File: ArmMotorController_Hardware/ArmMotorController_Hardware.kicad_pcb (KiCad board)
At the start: 2 copper layers, 124.5 x 121.9 mm, 110 parts, among them SW1 SW_Push, SW2 SW_Push, SW3 SW_Push, SW4 SW_Push, SW5 SW_SPDT, U1 AP1059, U2 AP1059, U3 TM4C129E_Launchpad, U4 MAX_3232, U5 VNH5019A_E, U6 VNH5019A_E, U7 VNH5019A_E, U8 VNH5019A_E

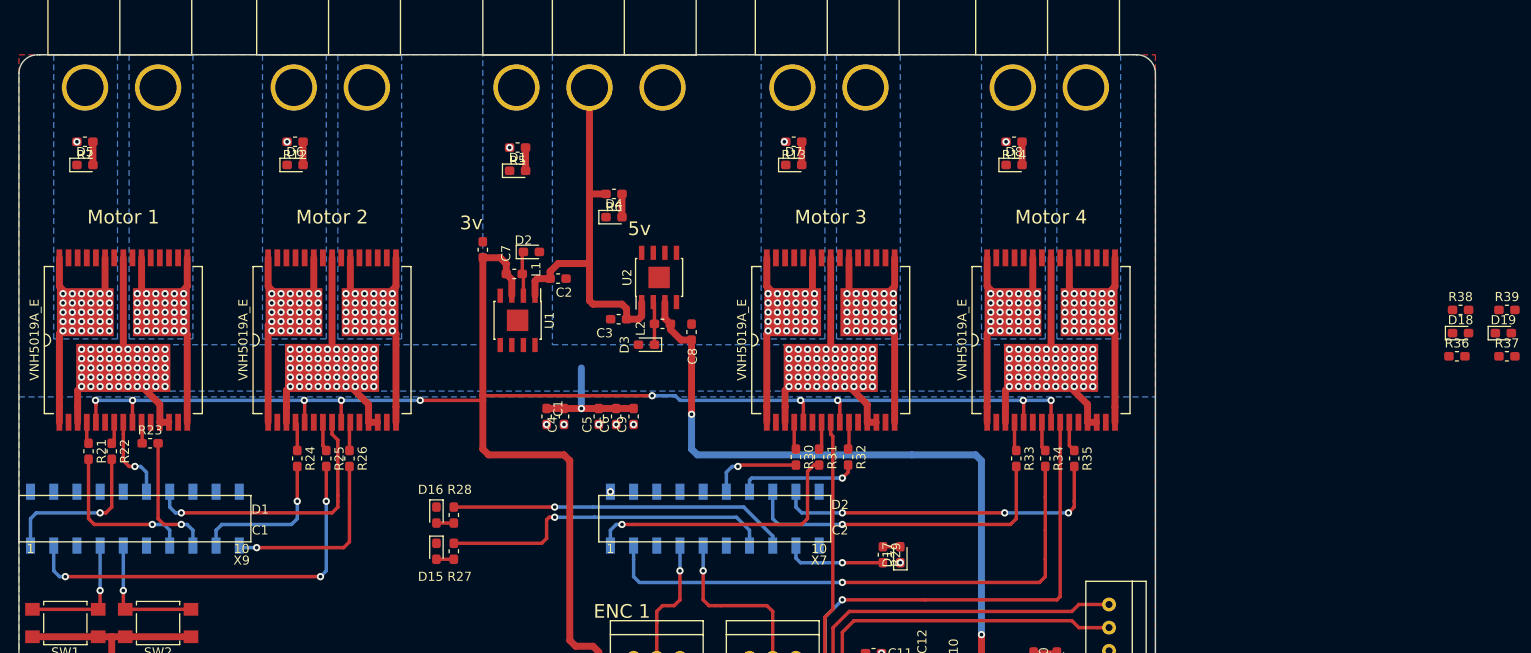
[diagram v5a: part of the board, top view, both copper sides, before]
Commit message: Began moving the new schematic change into place and added a junction to the schematic
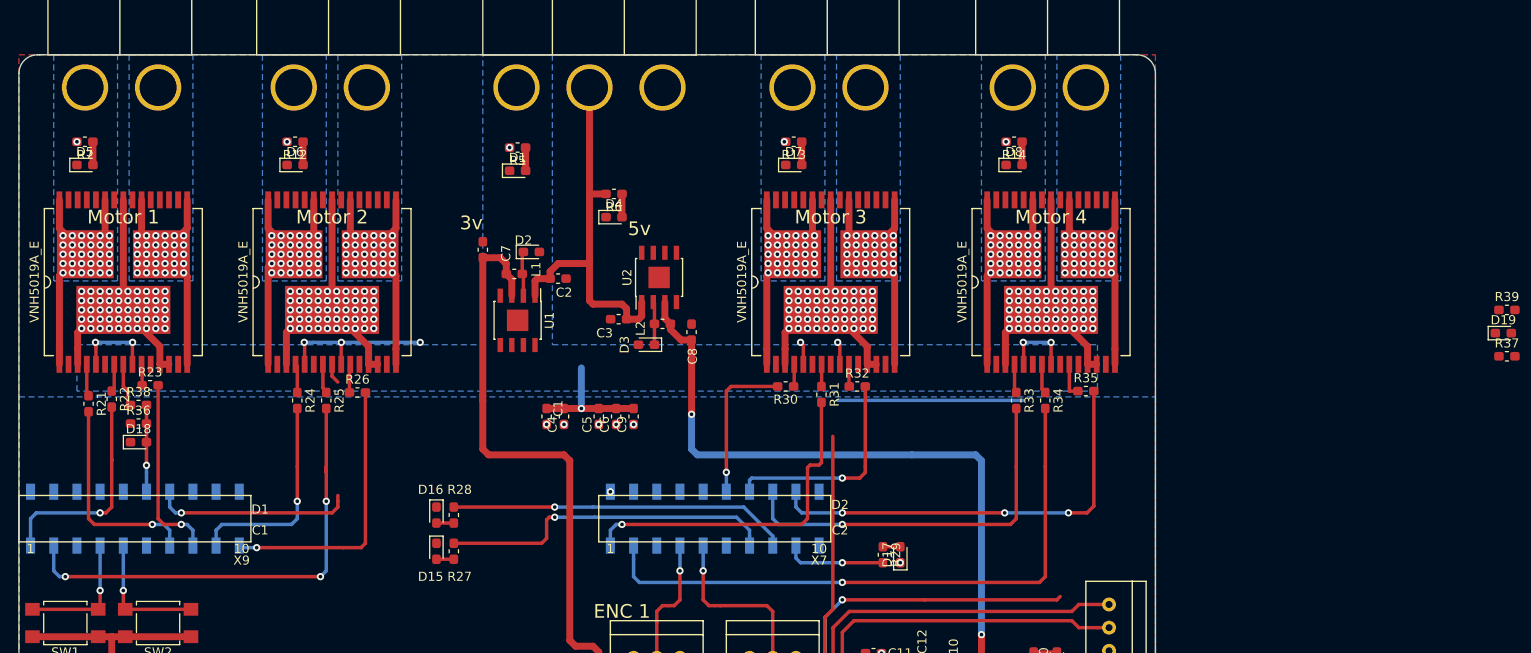
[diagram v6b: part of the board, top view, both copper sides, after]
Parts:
- moved D18 145.3 mm to (52.5, 84.3)
- moved R38 145.2 mm to (52.5, 80.3)
- moved R36 144.6 mm to (52.5, 82.3)
- moved R30 7.81 mm to (123.3, 78.2), turned to 180 degrees
- moved R32 7.80 mm to (131.2, 78.2), turned to 0 degrees
- moved R35 7.49 mm to (156.2, 78.7), turned to 0 degrees
- moved R26 7.28 mm to (76.4, 78.9), turned to 0 degrees
- moved R31 6.86 mm to (127.3, 79.1)
- moved R24 6.35 mm to (69.8, 79.8)
- moved R25 6.35 mm to (73.0, 79.8)
- moved R33 6.35 mm to (148.6, 79.8)
- moved R34 6.35 mm to (151.8, 79.8)
- moved R23 6.35 mm to (53.7, 78.1)
- moved U5 6.35 mm to (50.8, 66.8)
- moved U6 6.35 mm to (73.7, 66.8)
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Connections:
- D18 pad 2: Net-(D18-Pad2) -> I_Sense_1
- D19 pad 2: Net-(D19-Pad2) -> I_Sense_2
- D20 pad 2: Net-(D20-Pad2) -> I_Sense_3
- D21 pad 2: Net-(D21-Pad2) -> I_Sense_4
- R36 pad 2: Net-(D18-Pad2) -> I_Sense_1
- R37 pad 2: Net-(D19-Pad2) -> I_Sense_2
- R40 pad 2: Net-(D20-Pad2) -> I_Sense_3
- R41 pad 2: Net-(D21-Pad2) -> I_Sense_4
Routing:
- net +3V3: track 454.6 -> 389.9 mm, vias 12 -> 11
- net I_Sense_4: track 85.3 -> 66.2 mm
- net IN_B3: track 13.2 -> 23.7 mm
- net IN_B4: track 37.1 -> 47.5 mm
- net IN_B2: track 20.7 -> 30.6 mm
- net I_Sense_2: track 30.2 -> 21.9 mm
- net Mo3_PWM: track 30.5 -> 37.7 mm
- net Mo2_PWM: track 44.6 -> 51.6 mm
- net IN_A3: track 10.1 -> 16.9 mm
- net Mo4_PWM: track 61.1 -> 67.4 mm
- net IN_A4: track 35.9 -> 42.2 mm
- net IN_A2: track 16.8 -> 23.2 mm
- net IN_B1: track 14.3 -> 20.6 mm
- net Mo1_PWM: track 17.6 -> 23.5 mm
- net IN_A1: track 17.2 -> 22.8 mm
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
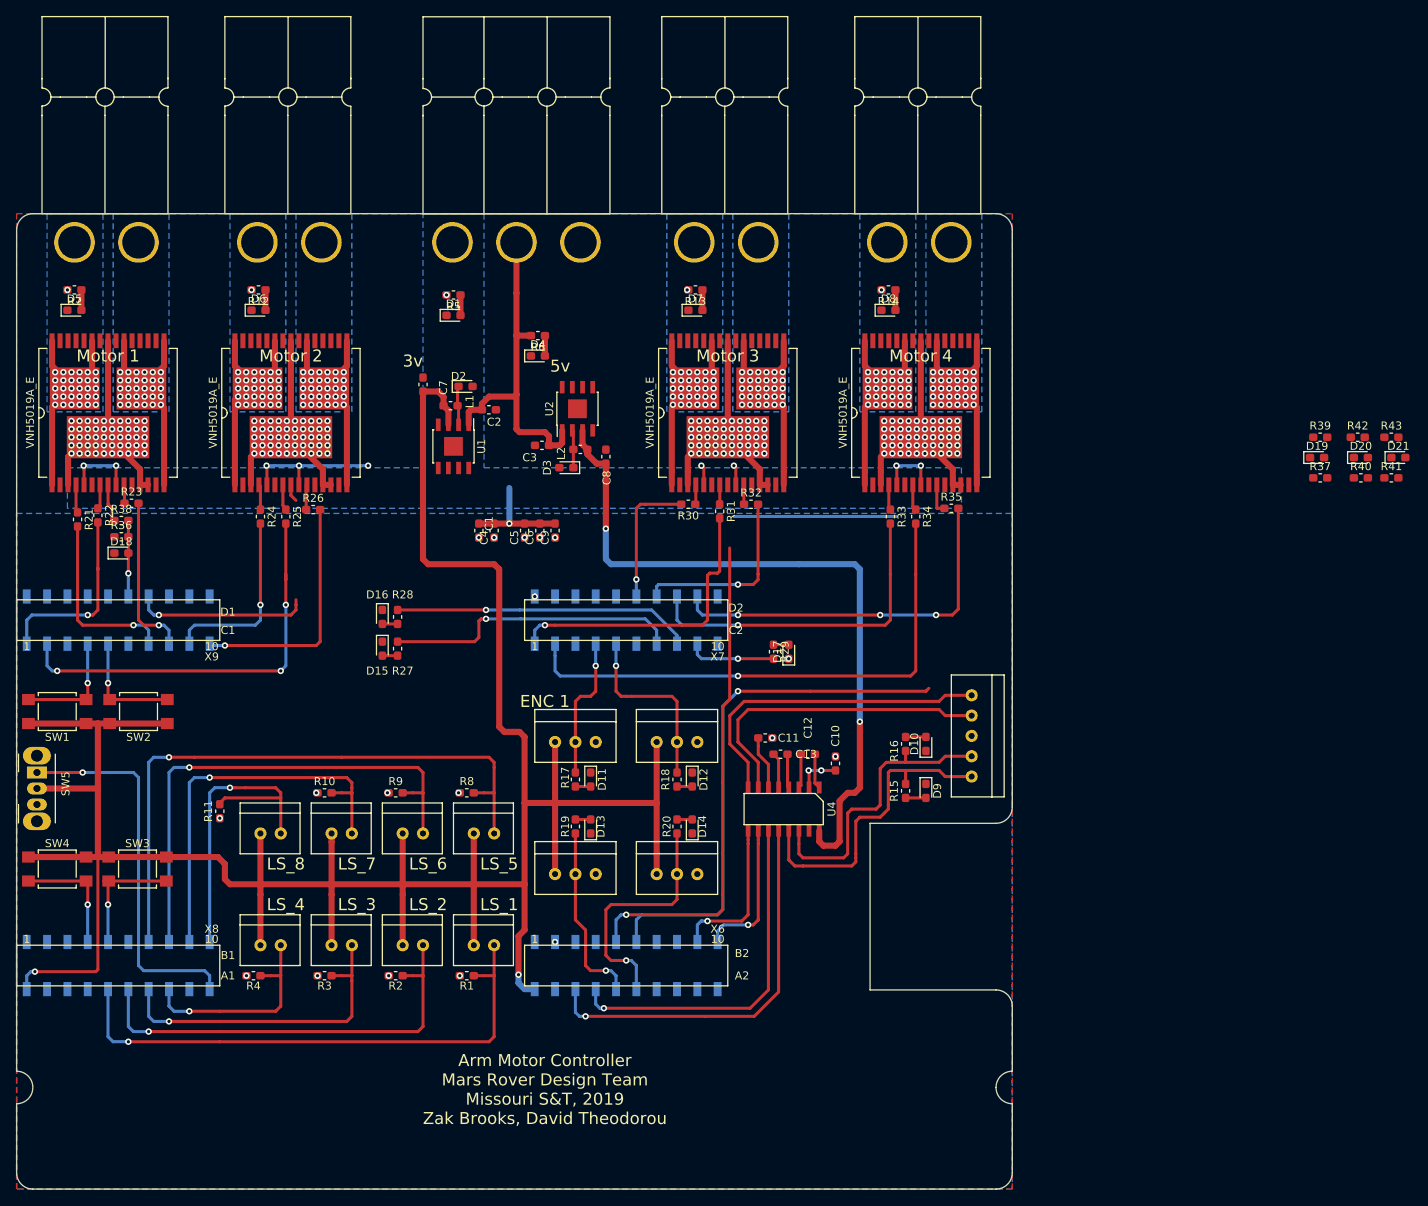
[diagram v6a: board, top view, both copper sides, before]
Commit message: Finished attaching the new circuit and made sure everything was connected
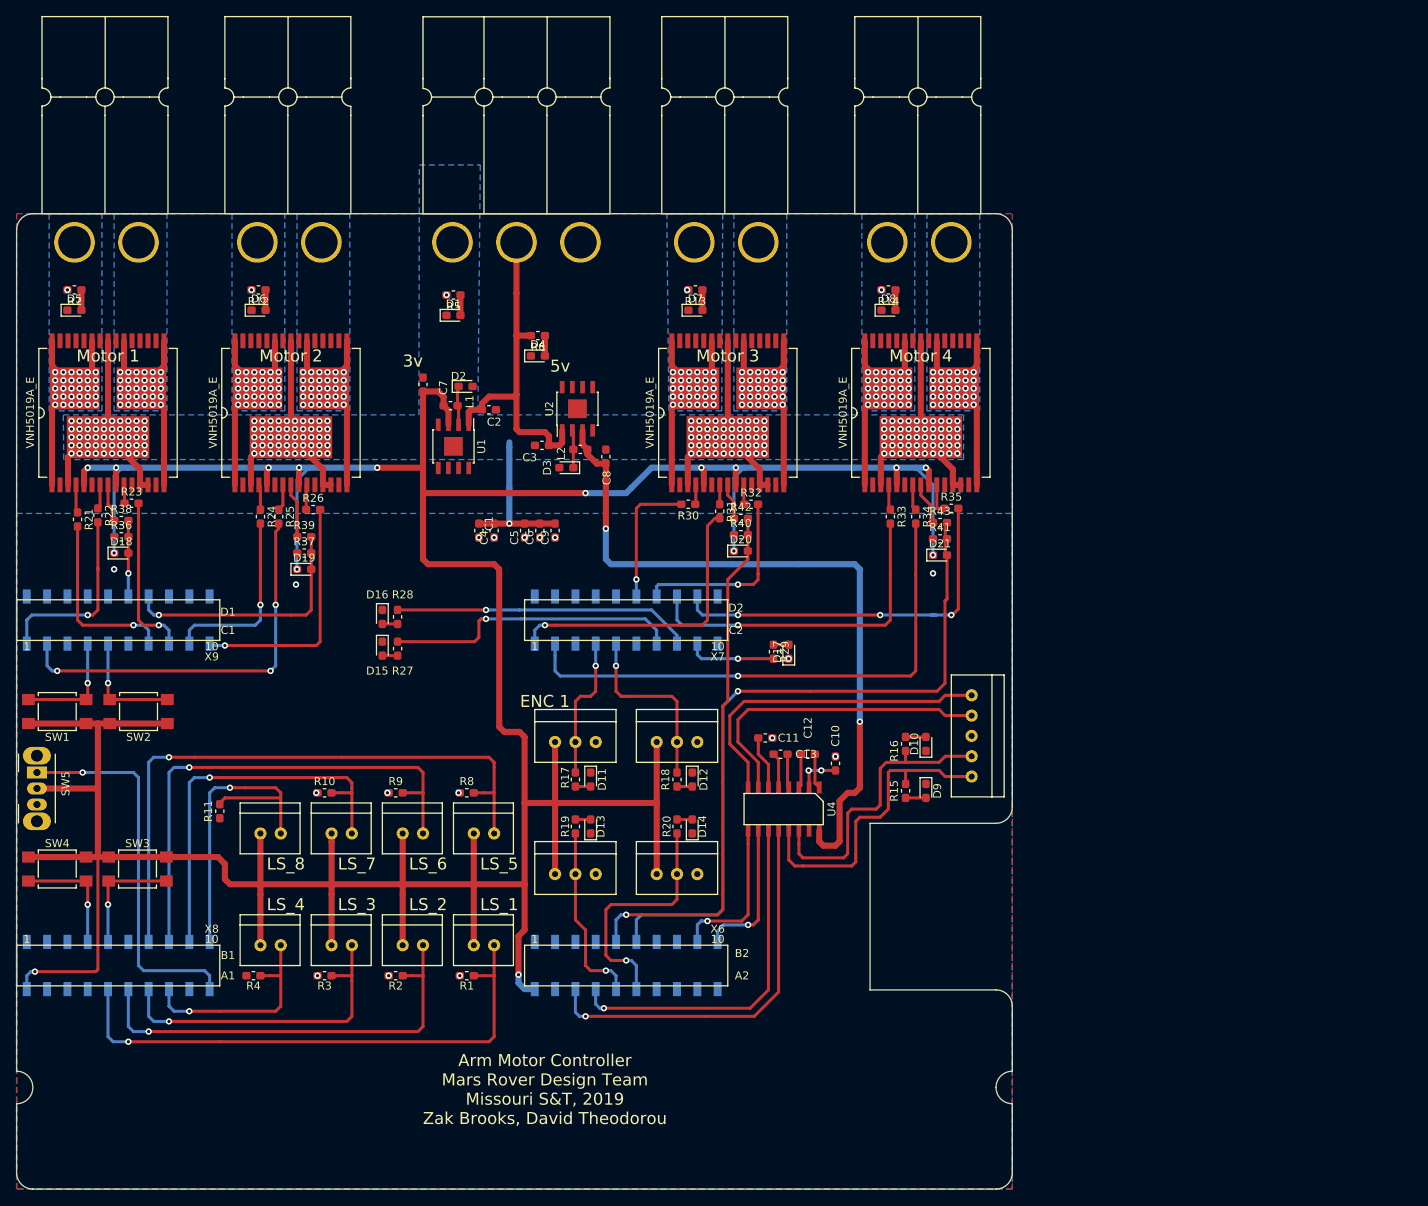
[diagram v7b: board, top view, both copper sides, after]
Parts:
- moved R39 127.6 mm to (75.3, 82.3)
- moved D19 127.4 mm to (75.3, 86.4)
- moved R37 127.3 mm to (75.3, 84.3)
- moved D20 78.4 mm to (129.9, 84.1)
- moved R40 77.8 mm to (129.9, 82.0)
- moved R42 77.8 mm to (129.9, 80.0)
- moved D21 58.6 mm to (154.8, 84.6)
- moved R43 57.4 mm to (154.8, 80.5)
- moved R41 56.9 mm to (154.8, 82.5)
- moved R25 0.89 mm to (72.1, 79.8)
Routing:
- net +3V3: track 389.9 -> 501.3 mm, vias 11 -> 16
- net I_Sense_4: track 66.2 -> 88.7 mm
- net I_Sense_2: track 21.9 -> 31.7 mm
- net 12vAct: track 136.2 -> 141.9 mm
- net Net-(R43-Pad1): track 0.00 -> 5.25 mm
- net I_Sense_3: track 62.2 -> 66.8 mm
- net Net-(R39-Pad1): track 2.21 -> 6.82 mm
- net Net-(R42-Pad1): track 0.00 -> 4.52 mm
- net Mo2_PWM: track 51.6 -> 49.8 mm
- net IN_B4: track 47.5 -> 48.1 mm
- net GND: vias 19 -> 18

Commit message: FInished the schematic changes and attched them on the PCB
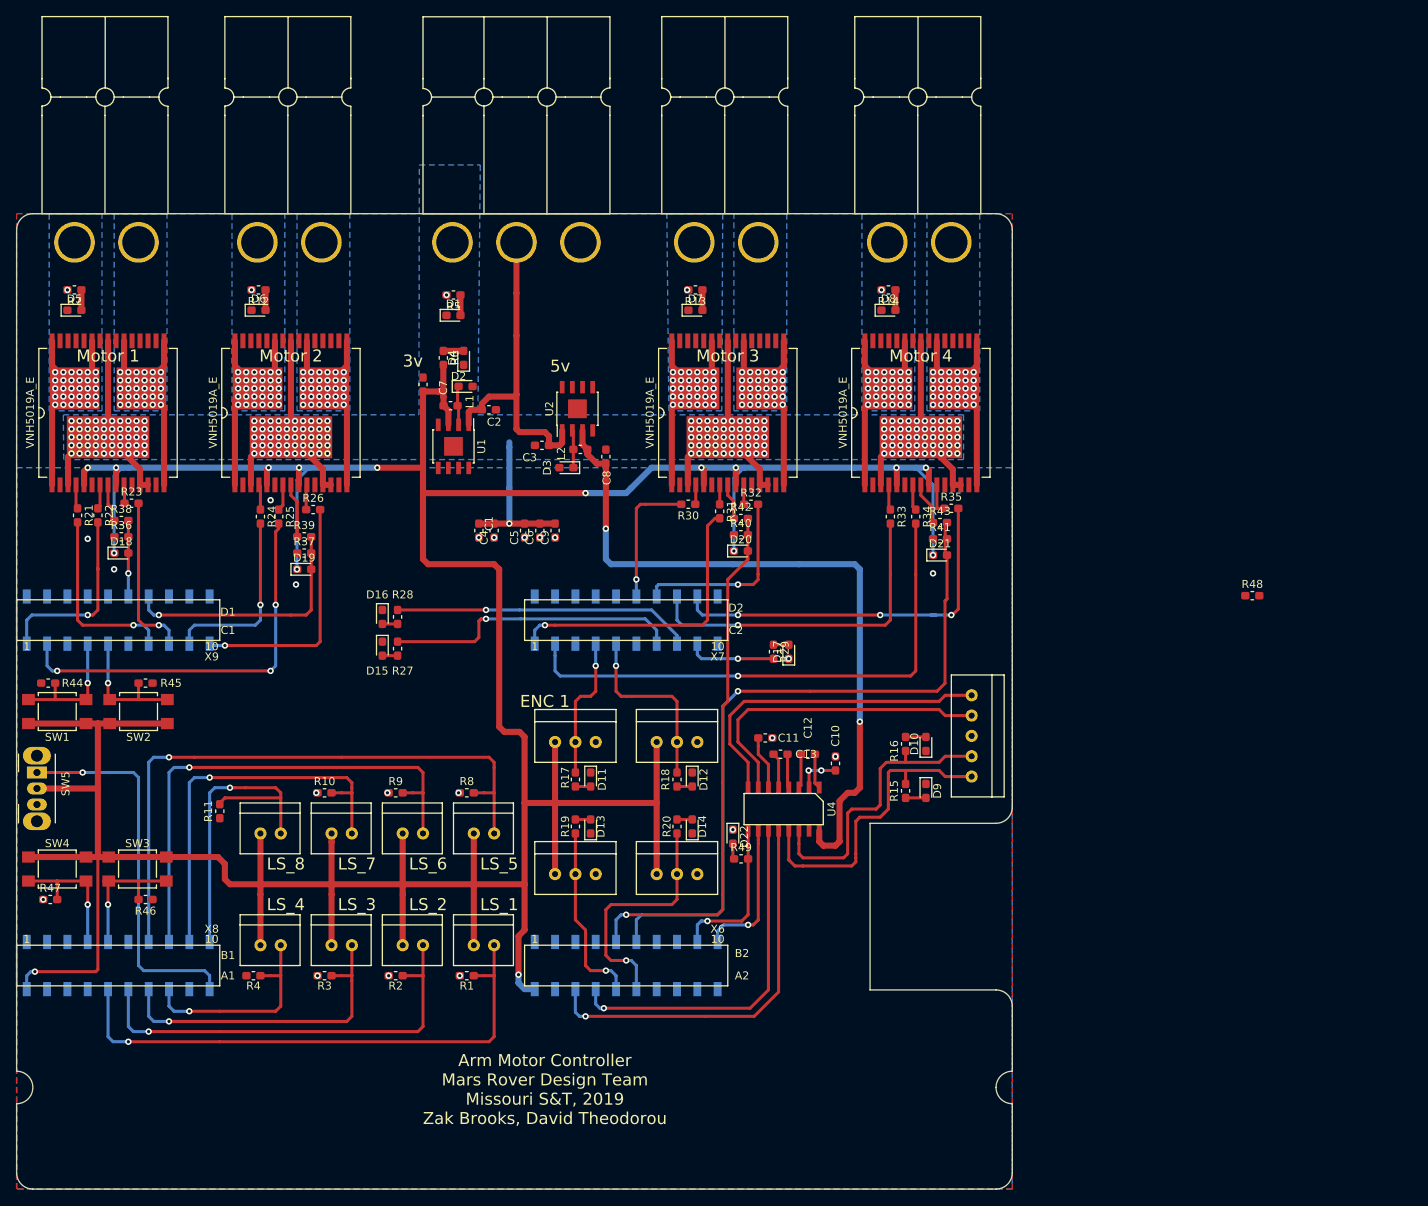
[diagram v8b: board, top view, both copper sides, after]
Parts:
- added D22: LED, LED_SMD:LED_0603_1608Metric_Pad1.05x0.95mm_HandSolder, F.Cu at (128.9, 119.8)
- added R44: 500, Resistor_SMD:R_0603_1608Metric_Pad1.05x0.95mm_HandSolder, F.Cu at (43.3, 100.6)
- added R45: 500, Resistor_SMD:R_0603_1608Metric_Pad1.05x0.95mm_HandSolder, F.Cu at (55.5, 100.6)
- added R46: 500, Resistor_SMD:R_0603_1608Metric_Pad1.05x0.95mm_HandSolder, F.Cu at (55.5, 127.6)
- added R47: 500, Resistor_SMD:R_0603_1608Metric_Pad1.05x0.95mm_HandSolder, F.Cu at (43.6, 127.6)
- added R48: 500, Resistor_SMD:R_0603_1608Metric_Pad1.05x0.95mm_HandSolder, F.Cu at (193.8, 89.7)
- added R49: 500, Resistor_SMD:R_0603_1608Metric_Pad1.05x0.95mm_HandSolder, F.Cu at (129.9, 122.6)
- moved R6 12.1 mm to (92.7, 59.9), turned to 270 degrees
- moved D4 9.29 mm to (95.2, 59.9), turned to 90 degrees
- moved R21 0.51 mm to (47.0, 79.6)
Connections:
- net 12vAct renamed +12V
- net ENC_1 renamed ENC_1_PWM
- net ENC_2 renamed ENC_2_PWM
- net ENC_3 renamed ENC_3_PWM
- net ENC_4 renamed ENC_4_PWM
- net I_Sense_1 renamed I_SENSE_1
- net I_Sense_2 renamed I_SENSE_2
- net I_Sense_3 renamed I_SENSE_3
- net I_Sense_4 renamed I_SENSE_4
- net LED_1 renamed LED_IND_SW_1
- net LED_2 renamed LED_IND_SW_2
- net LED_3 renamed LED_IND_SW_3
- net Net-(Conn16-Pad2) renamed /Out_B1M1
- net Net-(Conn17-Pad2) renamed /Out_B2M2
- net Net-(Conn18-Pad2) renamed /Out_B3M3
- net Net-(Conn19-Pad2) renamed /Out_B4M4
- net Net-(R38-Pad1) renamed I_SENSE_SW_1
- net Net-(R39-Pad1) renamed I_SENSE_SW_2
- net Net-(R42-Pad1) renamed I_SENSE_SW_3
- net Net-(R43-Pad1) renamed I_SENSE_SW_4
- R6 pad 2: 12vLog -> +3V3
- U5 pad 6: Net-(U5-Pad6) -> GND
- U6 pad 6: Net-(U6-Pad6) -> GND
- U7 pad 6: Net-(U7-Pad6) -> GND
- U8 pad 6: Net-(U8-Pad6) -> GND
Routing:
- net +3V3: track 501.3 -> 505.0 mm
- net Mo4_SW: track 14.9 -> 17.2 mm
- net Mo3_SW: track 14.9 -> 17.2 mm
- net Mo2_SW: track 14.3 -> 16.3 mm
- net Mo1_SW: track 14.3 -> 16.3 mm
- net Net-(D22-Pad2): track 0.00 -> 1.97 mm
- net 12vLog: track 43.0 -> 41.2 mm
- net Net-(R21-Pad1): track 3.52 -> 3.01 mm
- net IN_A1: track 22.8 -> 23.3 mm
- net GND: vias 18 -> 22
